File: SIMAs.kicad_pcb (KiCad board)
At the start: 2 copper layers, 78 parts, among them J1 USB_C_Receptacle_PowerOnly_6P, J2 Conn_01x02_Socket, J3 Conn_01x04_Socket, J4 Conn_01x04_Socket, J5 Conn_01x04_Socket, J6 Conn_01x03_Socket, J7 Conn_01x02_Socket, J8 Conn_01x02_Socket, Q1 QM6015D, U1 mini_esp32, U2 BQ25628ERYKR, U3 TPS611781RNWR, U4 TLV61070ADBV, U5 CNY70, U6 CNY70, U7 CNY70, U8 DRV8876PWPR, U9 DRV8876PWPR

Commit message: actualitzar ultrima versio pcb/esquematic
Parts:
- moved U2 7.71 mm to (96.6, 26.9)
- moved C4 0.38 mm to (86.1, 43.0)
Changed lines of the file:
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@@
 	(footprint "BQ25628E:WQFN-HR18__RYK_TEX"
 		(layer "F.Cu")
-		(at 100.925001 20.45)
+		(at 96.624999 26.85)
 		(tags "BQ25628ERYKR ")
 		(property "Reference" "U2"
@@
 	(footprint "Capacitor_SMD:C_0603_1608Metric_Pad1.08x0.95mm_HandSolder"
 		(layer "F.Cu")
-		(at 86.515002 43.035001)
+		(at 86.1375 43.035001)
 		(descr "Capacitor SMD 0603 (1608 Metric), square (rectangular) end terminal, IPC_7351 nominal with elongated pad for handsoldering. (Body size source: IPC-SM-782 page 76, https://www.pcb-3d.com/wordpress/wp-content/uploads/ipc-sm-782a_amendment_1_and_2.pdf), generated with kicad-footprint-generator")
 		(tags "capacitor handsolder")

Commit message: arreclat footprints/symbol
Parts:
- R20: footprint Mounting_Wuerth:Mounting_Wuerth_WA-SMSE-ExternalM3_H6mm_9771060360 -> Resistor_SMD:R_0603_1608Metric
- U3: footprint TPS61178:RNW0013A -> tps611781rnwr:RNW0013A
- U8: footprint DRV8876:PWP0016J_N -> dvr8876pwpr:PWP0016J_N
- U9: footprint BQ25628E:WQFN-HR18__RYK_TEX -> dvr8876pwpr:PWP0016J_N

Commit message: esquematic fet v1
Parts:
- C10, C11, C12, C13, C14, C15, C16, C17, C18, C19, C20, C21, C22, C23, C24, C8, C9: footprint Capacitor_SMD:C_0201_0603Metric -> Capacitor_SMD:C_0603_1608Metric_Pad1.08x0.95mm_HandSolder
- R1, R10, R11, R12, R13, R14, R15, R16, R17, R18, R19, R2, R21, R22, R23, R24, R25, R26, R27, R28, R29, R3, R30, R4, R5, R6, R7, R8, R9: footprint Resistor_SMD:R_0201_0603Metric -> Resistor_SMD:R_0603_1608Metric

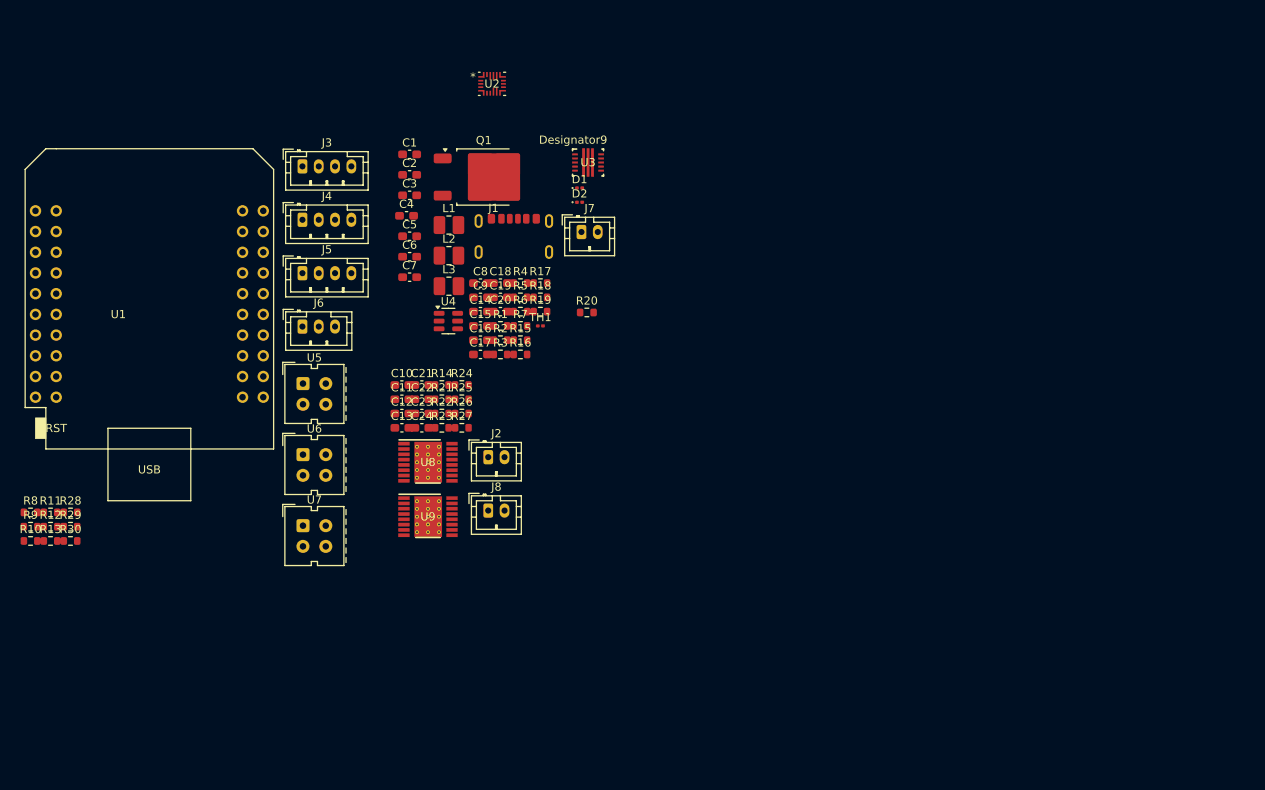
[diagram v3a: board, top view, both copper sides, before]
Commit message: Col·locats tots els components
S'han col·locat tots els components a la seva posició a la placa a més d'haver-ne afegit algun més.
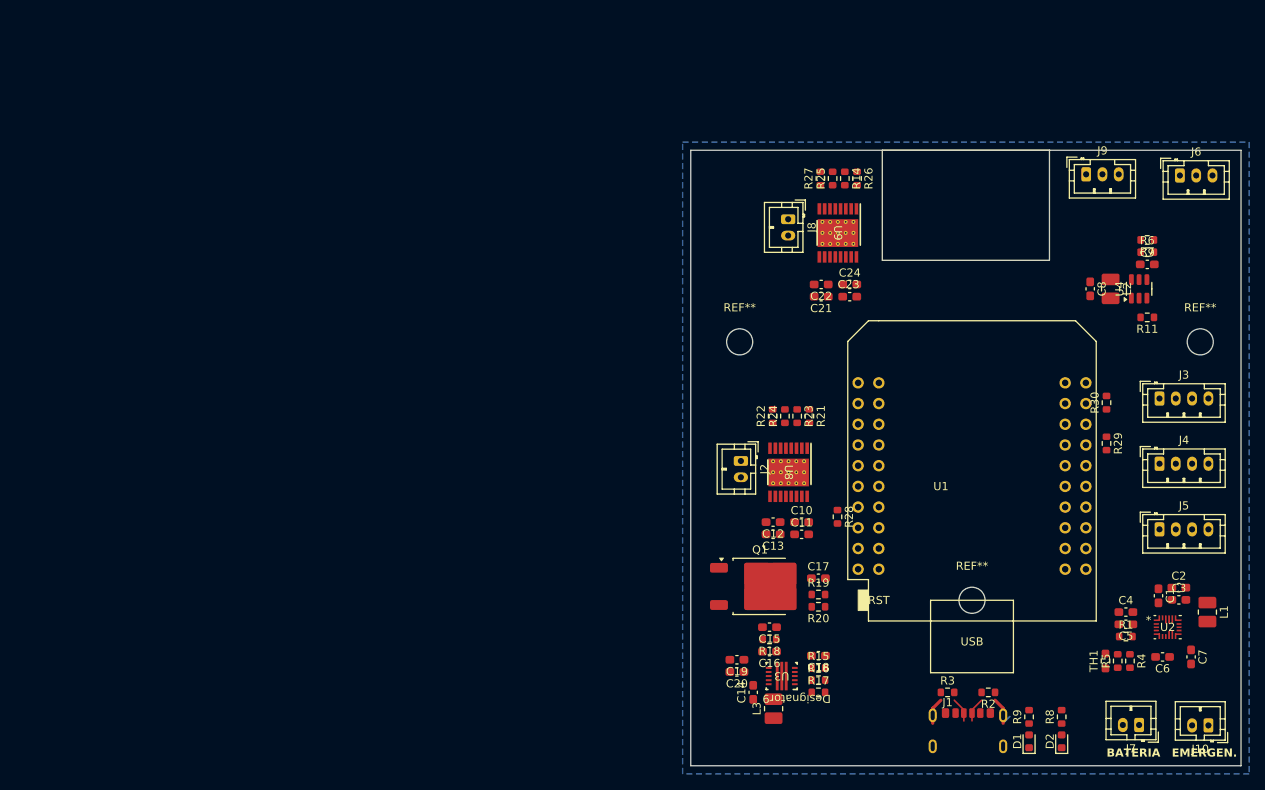
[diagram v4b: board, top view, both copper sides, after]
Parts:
- removed R10, R12: 110, Resistor_SMD:R_0603_1608Metric
- removed R13: 2,2 k, Resistor_SMD:R_0603_1608Metric
- removed U5, U6, U7: CNY70, OptoDevice:Vishay_CNY70
- added J10: Conn_01x02_Pin, Connector_JST:JST_PH_B2B-PH-K_1x02_P2.00mm_Vertical, F.Cu at (184.5, 105.5)
- added J9: Conn_01x03_Socket, Connector_JST:JST_PH_B3B-PH-K_1x03_P2.00mm_Vertical, F.Cu at (169.5, 38.0)
- added REF**: MountingHole_3.2mm_M3, MountingHole:MountingHole_3.2mm_M3, F.Cu at (183.5, 58.5)
- added REF**: MountingHole_3.2mm_M3, MountingHole:MountingHole_3.2mm_M3, F.Cu at (155.5, 90.2)
- added REF**: MountingHole_3.2mm_M3, MountingHole:MountingHole_3.2mm_M3, F.Cu at (127.0, 58.5)
- D1, D2: footprint Diode_SMD:D_0201_0603Metric -> Diode_SMD:D_0603_1608Metric
- J7: value Conn_01x02_Socket -> Bateria
- R11: value 2,2 k -> 732 k
- R28, R29, R30: value 110 -> 4.7k
- R8: value 110 -> 10 k
- R9: value 2,2 k -> 10 k
- TH1: footprint Resistor_SMD:R_0201_0603Metric -> Resistor_SMD:R_0603_1608Metric_Pad0.98x0.95mm_HandSolder
- moved R11 136.6 mm to (177.0, 55.5), turned to 180 degrees
- moved R8 128.9 mm to (166.5, 104.5), turned to 90 degrees
- moved R30 128.2 mm to (172.0, 66.0), turned to 90 degrees
- moved R29 127.5 mm to (172.0, 71.0), turned to -90 degrees
- moved R9 124.7 mm to (162.5, 104.5), turned to 90 degrees
- moved J5 109.7 mm to (178.5, 81.5)
- moved J4 109.3 mm to (178.5, 73.5)
- moved J6 109.2 mm to (181.0, 38.1)
- moved J3 108.9 mm to (178.5, 65.5)
- moved C2 107.1 mm to (180.9, 88.7)
- moved C1 106.6 mm to (178.4, 89.7), turned to -90 degrees
- moved C3 106.6 mm to (180.9, 90.2)
- moved C7 106.6 mm to (182.4, 97.2), turned to -90 degrees
- moved U2 106.4 mm to (179.5, 93.5)
- moved C6 104.6 mm to (178.9, 97.2), turned to 180 degrees
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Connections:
- net /PH/IN4 renamed /EN/IN4
- C20 pad 1: vsys -> /VSys
- C7 pad 1: /Alimentació/VSYS -> /VSys
- C8 pad 1: /Alimentació/VSYS -> /VSys
- D1 pad 2: /Alimentació/SYS -> Net-(D1-A)
- D2 pad 2: /Alimentació/SYS -> Net-(D2-A)
- L1 pad 2: /Alimentació/VSYS -> /VSys
- L2 pad 1: /Alimentació/VSYS -> /VSys
- L3 pad 1: vsys -> /VSys
- R11 pad 1: /SENSE_LLUM_2 -> EM_BTN
- R11 pad 2: +3.3V -> GND
- R28 pad 1: /Alimentació//INT -> /nFAULT2
- R8 pad 1: Net-(U5-A) -> Net-(D2-A)
- R8 pad 2: +3.3V -> /Alimentació/SYS
- R9 pad 1: /SENSE_LLUM_1 -> Net-(D1-A)
- R9 pad 2: +3.3V -> /Alimentació/SYS
- U1 pad 10: unconnected-(U1-IO_19/D6-Pad10) -> /FIDECURSA
- U1 pad 29: /Alimentació//INT -> /nFAULT2
- U2 pad 11: /Alimentació//INT -> /nFAULT2
- U2 pad 9: /Alimentació/SYS -> /VSys
- U3 pad 11: vsys -> EM_BTN
- U3 pad 12: vsys -> /VSys
- U4 pad 3: /Alimentació/VSYS -> EM_BTN
- U4 pad 6: /Alimentació/VSYS -> /VSys
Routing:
- net GND: track 0.00 -> 7.62 mm
- net Net-(J1-CC2): track 0.00 -> 3.02 mm
- net Net-(J1-CC1): track 0.00 -> 3.02 mm
- added copper zone on B.Cu, net GND
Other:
- board outline added: 67.5 x 75.5 mm
- board text added: "BATERIA"
- board text added: "EMERGEN."

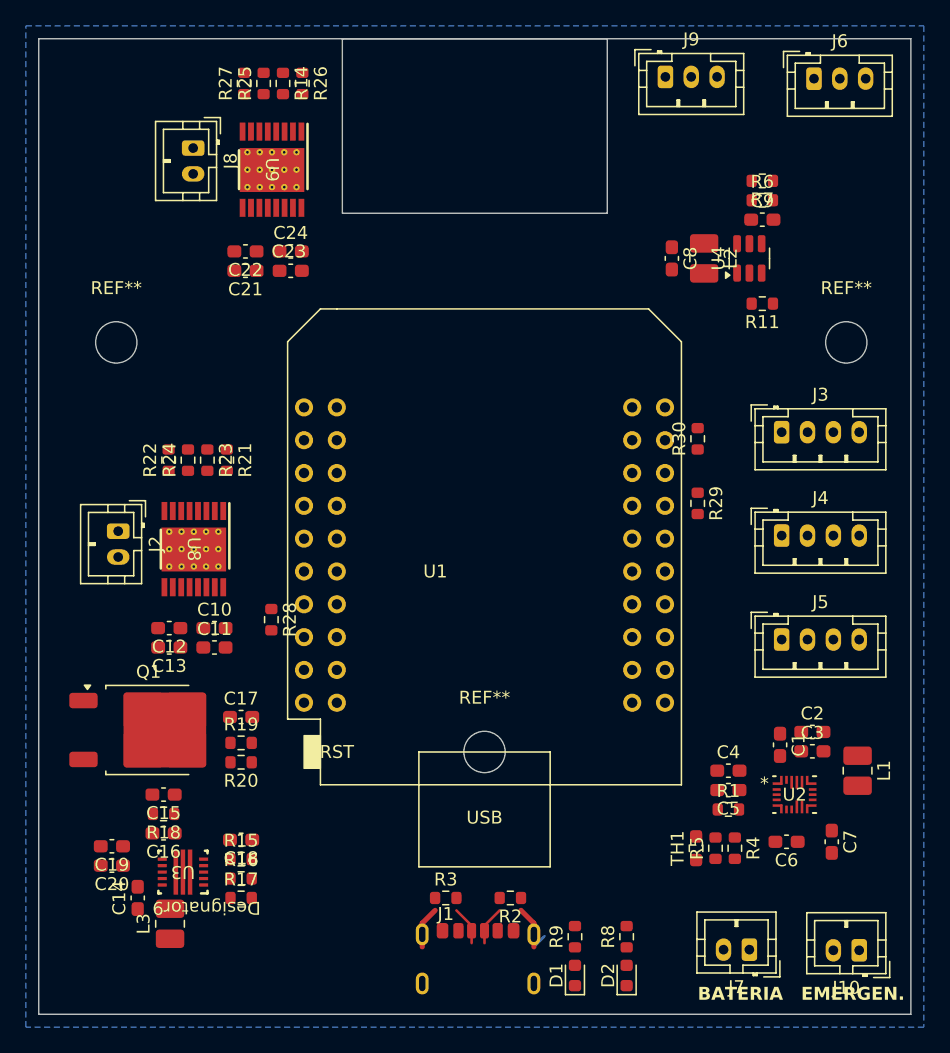
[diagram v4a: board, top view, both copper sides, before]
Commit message: Pistes
S'han fet les pistes i les connexions entre tots els components. Falta revisar-les.
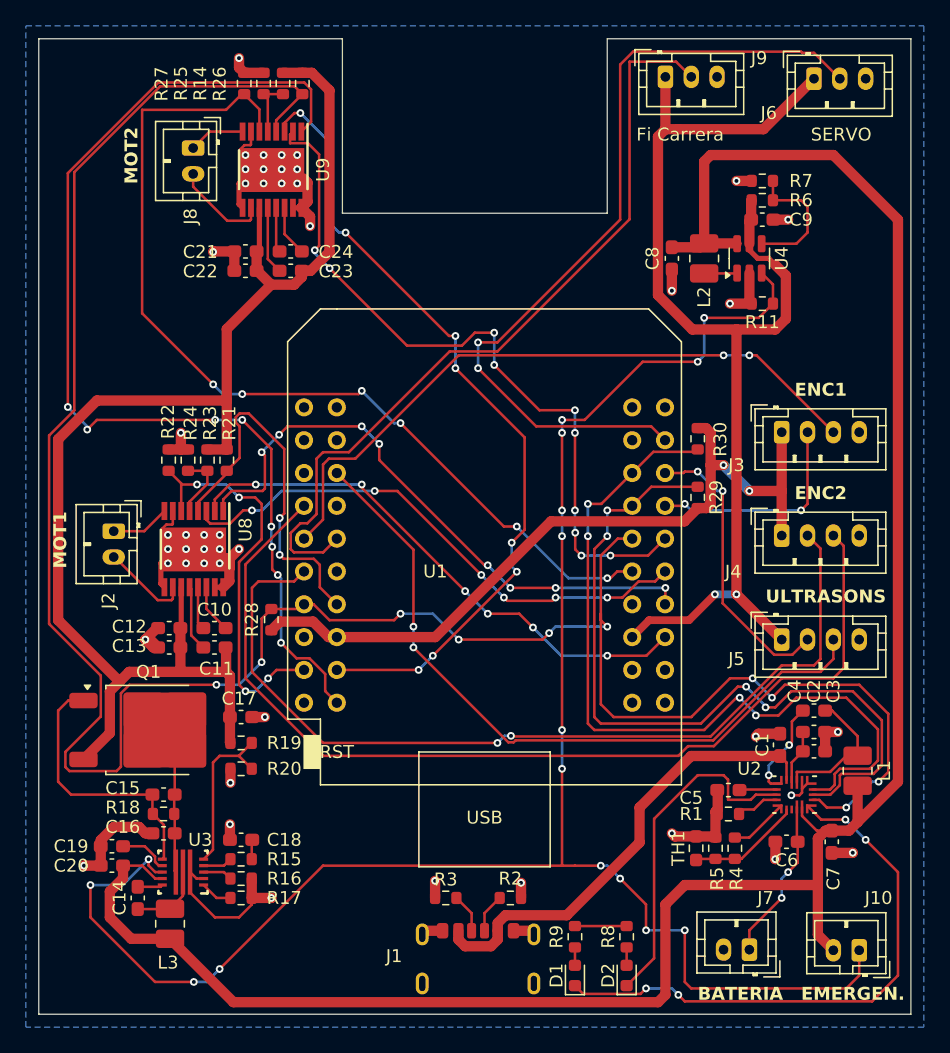
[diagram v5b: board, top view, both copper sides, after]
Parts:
- removed REF** (x3): MountingHole_3.2mm_M3, MountingHole:MountingHole_3.2mm_M3
- moved C4 8.09 mm to (181.0, 87.0), turned to 180 degrees
- moved R20 0.50 mm to (136.7, 91.5)
- moved R29 0.46 mm to (172.0, 70.5)
- moved R1 0.35 mm to (174.4, 95.0)
- moved J2 0.35 mm to (126.8, 73.1)
- moved C2 0.12 mm to (181.0, 88.7)
- moved C3 0.12 mm to (181.0, 90.2)
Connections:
- R21 pad 2: /Motors/nFAULT1 -> /nFAULT1
- R22 pad 1: /Motors/IPROPI1 -> /IPROPI1
- R26 pad 2: /Motors/nFAULT2 -> /nFAULT2
- R27 pad 1: /Motors/IPROPI2 -> /IPROPI2
- R28 pad 2: Net-(U1-3V3) -> +3.3V
- R29 pad 2: Net-(U1-3V3) -> +3.3V
- R30 pad 2: Net-(U1-3V3) -> +3.3V
- U1 pad 16: Net-(U1-3V3) -> +3.3V
- U8 pad 1: /Motors/EN/IN1 -> /EN/IN1
- U8 pad 2: /Motors/PH/IN2 -> /PH/IN2
- U8 pad 3: /Motors/nSLEEP1 -> /nSLEEP1
- U8 pad 4: /Motors/nFAULT1 -> /nFAULT1
- U8 pad 6: /Motors/IPROPI1 -> /IPROPI1
- U9 pad 1: /Motors/EN/IN3 -> /EN/IN3
- U9 pad 2: /Motors/PH/IN4 -> /EN/IN4
- U9 pad 3: /Motors/nSLEEP2 -> /nSLEEP2
- U9 pad 4: /Motors/nFAULT2 -> /nFAULT2
- U9 pad 6: /Motors/IPROPI2 -> /IPROPI2
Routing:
- net /nFAULT2: track 0.00 -> 182.0 mm, vias 0 -> 10
- net /VSys: track 0.00 -> 169.0 mm
- net EM_BTN: track 0.00 -> 143.7 mm, vias 0 -> 16
- net +12V: track 0.00 -> 109.7 mm
- net GND: track 7.62 -> 95.7 mm, vias 0 -> 47
- net +5V: track 0.00 -> 87.4 mm, vias 0 -> 2
- net /EN/IN3: track 0.00 -> 83.8 mm, vias 0 -> 8
- net /ENC4: track 0.00 -> 77.4 mm
- net /IPROPI2: track 0.00 -> 74.4 mm, vias 0 -> 6
- net /ENC3: track 0.00 -> 70.0 mm, vias 0 -> 2
- net /SERVO: track 0.00 -> 64.0 mm, vias 0 -> 2
- net /nSLEEP2: track 0.00 -> 63.1 mm, vias 0 -> 8
- net /Alimentació/SCL: track 0.00 -> 62.1 mm, vias 0 -> 4
- net /FIDECURSA: track 0.00 -> 61.6 mm
- net /Alimentació/SDA: track 0.00 -> 60.2 mm, vias 0 -> 4
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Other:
- board text added: "ENC1"
- board text added: "ENC2"
- board text added: "Fi Carrera"
- board text added: "MOT1"
- board text added: "MOT2"
- board text added: "SERVO"
- board text added: "ULTRASONS"

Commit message: Revisio de la placa
S'ha revisat la placa
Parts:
- added D3: WS2812B, LED_SMD:LED_WS2812B_PLCC4_5.0x5.0mm_P3.2mm, F.Cu at (126.5, 94.0)
- added D4: D, Diode_SMD:D_SMA_Handsoldering, F.Cu at (129.5, 88.0)
- added D5: 5 V, Diode_SMD:D_SOD-323, F.Cu at (164.6, 101.8)
- added D6: 5 V, Diode_SMD:D_SOD-323, F.Cu at (171.3, 49.9)
- added D7: 5 V, Diode_SMD:D_SOD-323, F.Cu at (130.1, 101.5)
- added D8: 3,3 V, Diode_SMD:D_SOD-323, F.Cu at (167.0, 51.5)
- added D9: 12 V, Diode_SMD:D_SOD-323, F.Cu at (134.8, 97.0)
- added J11: Conn_01x03_Pin, Connector_JST:JST_PH_B3B-PH-K_1x03_P2.00mm_Vertical, F.Cu at (125.0, 105.0)
- added J12: Conn_01x03_Pin, Connector_JST:JST_PH_B3B-PH-K_1x03_P2.00mm_Vertical, F.Cu at (135.0, 105.0)
- added J13: Conn_01x05_Pin, Connector_JST:JST_PH_B5B-PH-K_1x05_P2.00mm_Vertical, F.Cu at (151.0, 51.5)
- added J14: Conn_01x02_Pin, Connector_JST:JST_PH_B2B-PH-K_1x02_P2.00mm_Vertical, F.Cu at (145.0, 105.0)
- added R10: DNP, Resistor_SMD:R_0603_1608Metric, F.Cu at (131.5, 93.0)
- J7: footprint Connector_JST:JST_PH_B2B-PH-K_1x02_P2.00mm_Vertical -> Connector_AMASS:AMASS_XT30U-M_1x02_P5.0mm_Vertical
- moved L3 31.9 mm to (162.0, 95.5), turned to 180 degrees
- moved C14 31.0 mm to (159.5, 98.0), turned to 180 degrees
- moved C20 29.8 mm to (156.5, 99.0), turned to -90 degrees
- moved C19 28.4 mm to (155.0, 99.0), turned to -90 degrees
- moved U3 25.8 mm to (157.5, 94.5), turned to -90 degrees
- moved R17 25.6 mm to (159.5, 90.0), turned to 90 degrees
- moved R16 23.6 mm to (158.0, 90.0), turned to 90 degrees
- moved C16 23.4 mm to (154.0, 95.0), turned to 90 degrees
- moved R18 23.1 mm to (153.5, 98.5), turned to -90 degrees
- moved C15 21.9 mm to (152.0, 98.5), turned to -90 degrees
- moved R15 21.6 mm to (156.5, 90.0), turned to 90 degrees
- moved C18 19.6 mm to (155.0, 90.0), turned to -90 degrees
- moved Q1 16.2 mm to (143.3, 97.0)
- moved R20 15.8 mm to (152.5, 91.5), turned to 90 degrees
- moved R19 14.5 mm to (151.0, 91.5), turned to 90 degrees
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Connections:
- C6 pad 1: Net-(J7-Pin_1) -> Net-(J7-Pin_2)
- J7 pad 1: Net-(J7-Pin_1) -> GND
- J7 pad 2: GND -> Net-(J7-Pin_2)
- R21 pad 2: /nFAULT1 -> /nFAULT
- R26 pad 2: /nFAULT2 -> /nFAULT
- R28 pad 1: /nFAULT2 -> /Alimentació//INT
- R8 pad 2: /Alimentació/SYS -> /VSys
- R9 pad 2: /Alimentació/SYS -> /VSys
- U1 pad 11: /ENC3 -> /LINIA1
- U1 pad 12: unconnected-(U1-IO_23/D7-Pad12) -> /ENC1
- U1 pad 13: /nFAULT2 -> /SONS2
- U1 pad 14: /nFAULT1 -> /EN/IN4
- U1 pad 17: /IPROPI1 -> unconnected-(U1-IO_09/SD2-Pad17)
- U1 pad 18: /nSLEEP2 -> /SONS1
- U1 pad 20: /EN/IN3 -> unconnected-(U1-IO_10/SD3-Pad20)
- U1 pad 24: /SERVO -> /ENC4
- U1 pad 26: /SONS1 -> /ENC2
- U1 pad 28: /ENC1 -> /nSLEEP
- U1 pad 29: /nFAULT2 -> /Alimentació//INT
- U1 pad 30: /EN/IN4 -> /SERVO
- U1 pad 31: /IPROPI2 -> /LEDs
- U1 pad 32: /nSLEEP1 -> /EN/IN3
- U1 pad 4: unconnected-(U1-IO_36/SVP/A0-Pad4) -> /LINIA3
- U1 pad 6: /SONS2 -> /ENC3
- U1 pad 7: /ENC4 -> /LINIA2
- U1 pad 8: unconnected-(U1-IO_18/D5-Pad8) -> /EXT_GPIO
- U1 pad 9: /ENC2 -> /nFAULT
- U2 pad 11: /nFAULT2 -> /Alimentació//INT
- U2 pad 8: Net-(J7-Pin_1) -> Net-(J7-Pin_2)
- U8 pad 3: /nSLEEP1 -> /nSLEEP
- U8 pad 4: /nFAULT1 -> /nFAULT
- U9 pad 3: /nSLEEP2 -> /nSLEEP
- U9 pad 4: /nFAULT2 -> /nFAULT
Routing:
- net /nFAULT2: track 182.0 -> 0.00 mm, vias 10 -> 0
- net /nFAULT: track 0.00 -> 104.6 mm, vias 0 -> 4
- net /Alimentació//INT: track 0.00 -> 82.5 mm, vias 0 -> 10
- net /nSLEEP: track 0.00 -> 77.1 mm, vias 0 -> 18
- net /IPROPI2: track 74.4 -> 3.39 mm, vias 6 -> 0
- net /nSLEEP2: track 63.1 -> 0.00 mm, vias 8 -> 0
- net +3.3V: track 60.0 -> 119.9 mm, vias 2 -> 6
- net /ENC4: track 77.4 -> 19.8 mm, vias 0 -> 4
- net /LEDs: track 0.00 -> 56.0 mm, vias 0 -> 6
- net /VSys: track 169.0 -> 117.1 mm, vias 0 -> 4
- net +5V: track 87.4 -> 136.5 mm, vias 2 -> 4
- net /EXT_GPIO: track 0.00 -> 47.1 mm, vias 0 -> 4
- net /nSLEEP1: track 41.8 -> 0.00 mm, vias 6 -> 0
- net /LINIA1: track 0.00 -> 37.5 mm, vias 0 -> 8
- net /ENC2: track 51.8 -> 16.1 mm, vias 2 -> 4
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- added copper zone on F.Cu, net /VSys
- added copper zone on F.Cu, net GND
- added copper zone on B.Cu, net Net-(J7-Pin_2)
- added copper zone on F.Cu, net Net-(J7-Pin_2)
- added copper zone on F.Cu, net Net-(Q1-D)
- added copper zone on F.Cu, net Net-(U2-SW)
- added copper zone on F.Cu, net Net-(U3-SW)
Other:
- board text added: "Càr. QI"
- board text added: "GPIO"
- board text added: "LEDs"
- board text added: "Seg. linies"

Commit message: Silskreen
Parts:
- added G***: LOGO, Logo_wolvineers:wolvineers, B.Cu at (156.2, 74.8)
- added REF**: MountingHole_3mm, MountingHole:MountingHole_3mm, F.Cu at (184.8, 55.8)
- added REF**: MountingHole_3mm, MountingHole:MountingHole_3mm, F.Cu at (124.8, 55.0)
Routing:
- net /EN/IN3: track 92.8 -> 92.0 mm
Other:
- board text added: "FEDAC Wolvineers SIMAs 2024/25"
